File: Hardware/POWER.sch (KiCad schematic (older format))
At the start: 27 parts, among them J1 ATX24, J2 ATX24, P1 RCA_STEREO_JACK, P3 3.5mm_Audio, P4 3.5mm_Audio, Q2 BSS138, SW1 PWR_BTN, U2 LP38692, U3 PLR135/T10, U4 POM-3535L-3-R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

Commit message: Fixing schematic issues
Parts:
- removed D3, D4: LED, symbol LED-RESCUE-museV2
- removed J1, J2: ATX24, symbol ATX24
- removed R6, R7: 470, symbol R-RESCUE-museV2
- added P2: +12V, symbol CONN_01X01
- added P43: +5V, symbol CONN_01X01
- added P44: +12V_AUX, symbol CONN_01X01
- added P45: +5V_AUX, symbol CONN_01X01
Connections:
- net labels added: EDISON_RST_OUT
- net labels removed: +3.3V, ATX_PS_1_OK, ATX_PS_2_OK, ATX_PS_ON, EDISON_RST_OUT(1.8)
- wire segments 134 -> 79
- no-connect marks 9 -> 0
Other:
- note added: "Power Connectors"
- note removed: "ATX Power Connectors"
- note removed: "ATX Power Indicators"

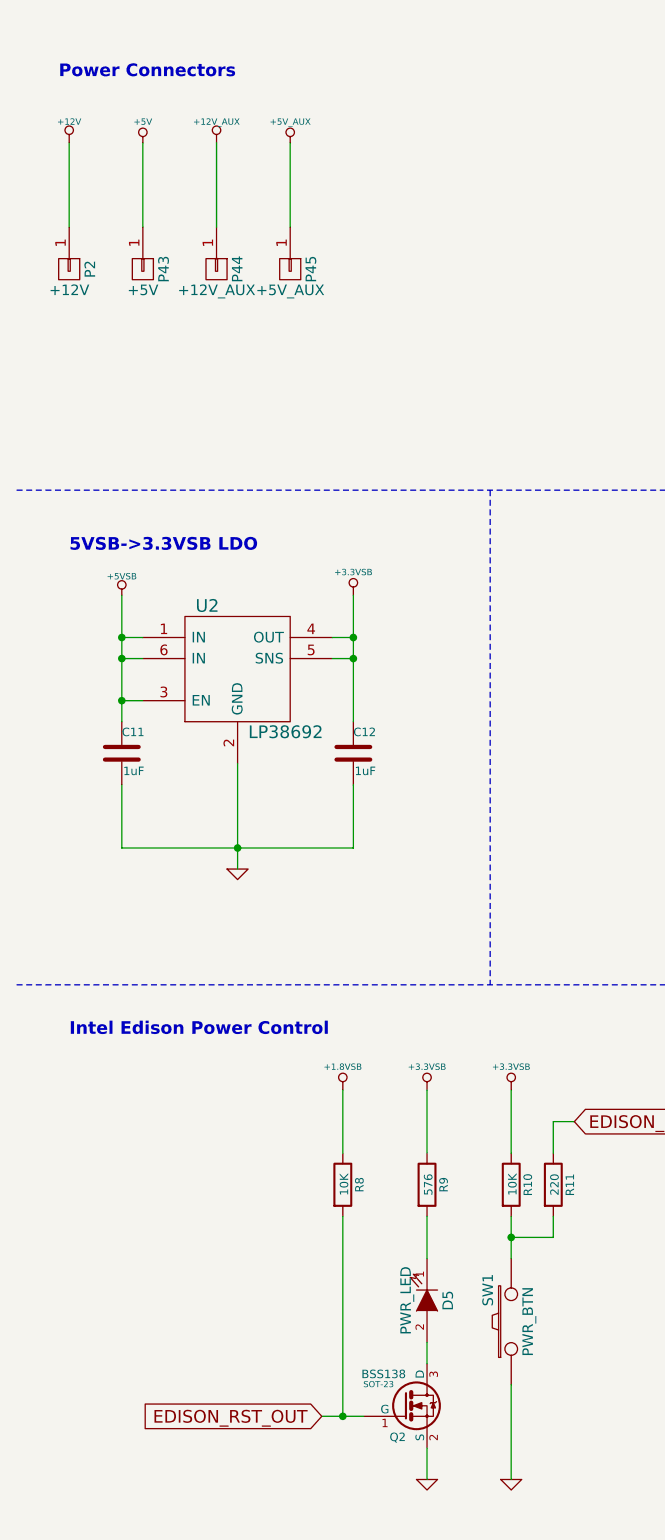
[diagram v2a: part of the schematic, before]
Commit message: Fixed schematic errors, added muse-v2-lib
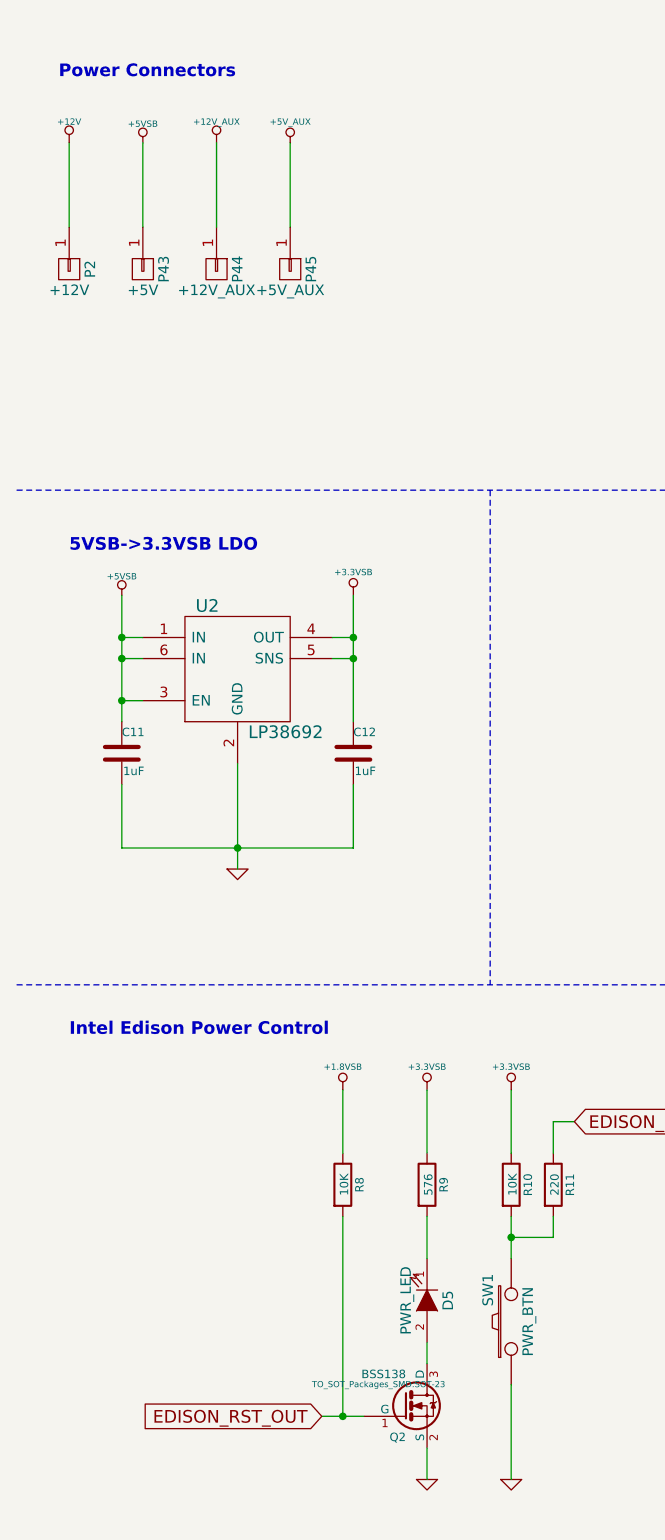
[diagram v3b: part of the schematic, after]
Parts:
- C11, C12, C13, C14: footprint (none) -> Capacitors_SMD:C_0402
- D5: footprint (none) -> LEDs:LED_0805
- P1: footprint (none) -> Choke_SMD:Choke_SMD_7.3x7.3_H3.5
- P43, P44, P45: footprint (none) -> Pin_Headers:Pin_Header_Straight_1x01
- Q2: footprint SOT-23 -> TO_SOT_Packages_SMD:SOT-23
- R10, R11, R8, R9: footprint (none) -> Resistors_SMD:R_0402
- SW1, U2, U3: footprint (none) -> MF_Switches:MF_Switches-TACT4.2MM
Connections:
- net +5V: no longer P43.1 (P1)
- net +5VSB: now also P43.1 (P1)

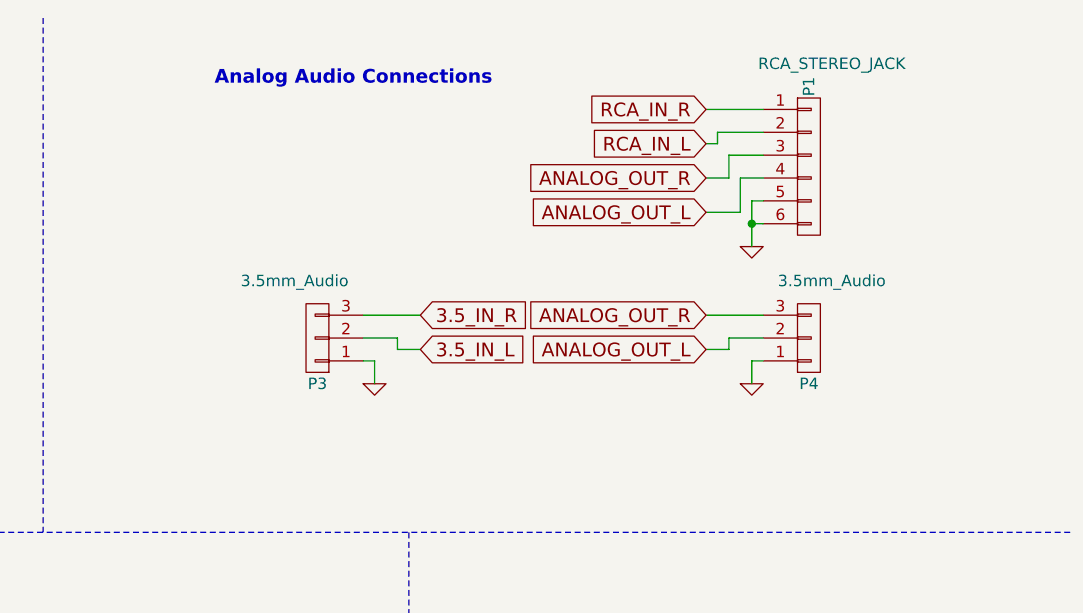
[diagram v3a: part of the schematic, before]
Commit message: Added proper audio connectors to schematic
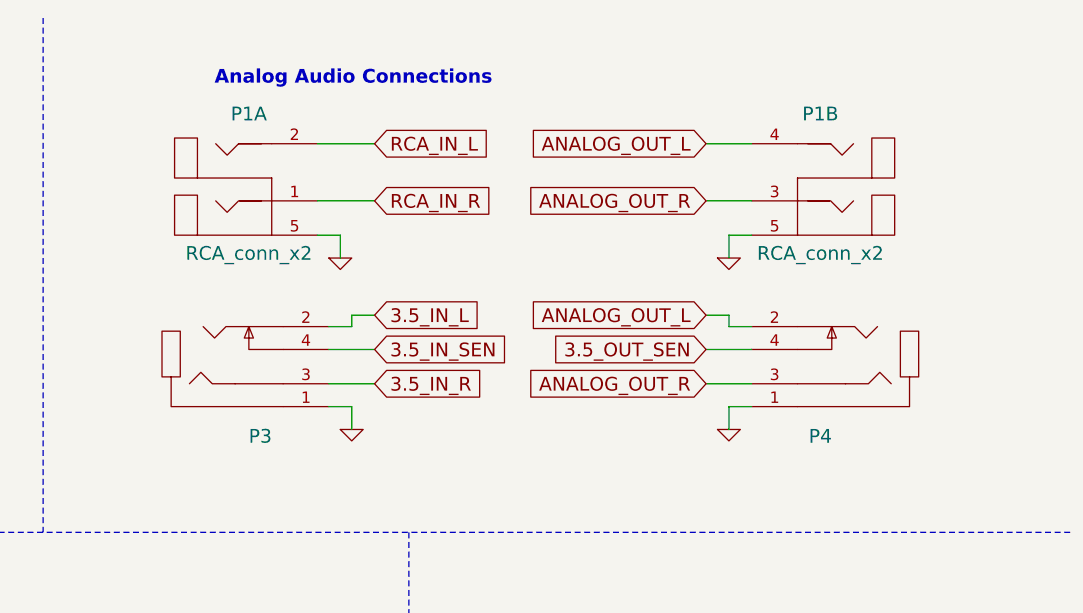
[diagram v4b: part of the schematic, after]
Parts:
- removed P1: RCA_STEREO_JACK, Choke_SMD:Choke_SMD_7.3x7.3_H3.5, symbol CONN_01X06
- removed P3, P4: 3.5mm_Audio, symbol CONN_01X03
- added P1: RCA_conn_x2, muse-v2-lib:PJRAS2X2S01X, symbol RCA_conn_x2
- added P3, P4: 3.5mm_conn_tip_switch, muse-v2-lib:3.5MM-AUDIO-SMD, symbol 3.5mm_conn_tip_switch
- P2: footprint (none) -> Pin_Headers:Pin_Header_Straight_1x01
- U2: footprint MF_Switches:MF_Switches-TACT4.2MM -> muse-v2-lib:WSON6
- U3: footprint MF_Switches:MF_Switches-TACT4.2MM -> muse-v2-lib:PLT133-T10W
- U4, U5, U7, U8: footprint (none) -> muse-v2-lib:POM-3535L-3-R
- U6: footprint (none) -> muse-v2-lib:PLT133-T10W
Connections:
- net 3.5_IN_L: now also P3.2
- net 3.5_IN_R: now also P3.3
- net ANALOG_OUT_L: now also P1.4, P4.2
- net ANALOG_OUT_R: now also P1.3, P4.3
- net GND: now also P1.5, P1.5, P3.1, P4.1
- net RCA_IN_L: now also P1.2
- net RCA_IN_R: now also P1.1
- new net 3.5_IN_SEN: P3.4
- new net 3.5_OUT_SEN: P4.4

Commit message: PCB Layout progress - placing PCM9211 components
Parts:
- U4, U5, U7, U8: footprint muse-v2-lib:POM-3535L-3-R -> muse-v2-lib:Pin_Header_Straight_1x02_MIC
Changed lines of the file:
@@
 F 0 "U4" H 9750 4100 60  0000 C CNN
 F 1 "POM-3535L-3-R" H 9900 3600 60  0000 C CNN
-F 2 "muse-v2-lib:POM-3535L-3-R" H 9900 3850 60  0001 C CNN
+F 2 "muse-v2-lib:Pin_Header_Straight_1x02_MIC" H 9900 3850 60  0001 C CNN
 F 3 "" H 9900 3850 60  0000 C CNN
 	1    9900 3850
@@
 F 0 "U5" H 9750 4700 60  0000 C CNN
 F 1 "POM-3535L-3-R" H 9900 4200 60  0000 C CNN
-F 2 "muse-v2-lib:POM-3535L-3-R" H 9900 4450 60  0001 C CNN
+F 2 "muse-v2-lib:Pin_Header_Straight_1x02_MIC" H 9900 4450 60  0001 C CNN
 F 3 "" H 9900 4450 60  0000 C CNN
 	1    9900 4450
@@
 F 0 "U7" H 9750 5300 60  0000 C CNN
 F 1 "POM-3535L-3-R" H 9900 4800 60  0000 C CNN
-F 2 "muse-v2-lib:POM-3535L-3-R" H 9900 5050 60  0001 C CNN
+F 2 "muse-v2-lib:Pin_Header_Straight_1x02_MIC" H 9900 5050 60  0001 C CNN
 F 3 "" H 9900 5050 60  0000 C CNN
 	1    9900 5050
@@
 F 0 "U8" H 9750 5900 60  0000 C CNN
 F 1 "POM-3535L-3-R" H 9900 5400 60  0000 C CNN
-F 2 "muse-v2-lib:POM-3535L-3-R" H 9900 5650 60  0001 C CNN
+F 2 "muse-v2-lib:Pin_Header_Straight_1x02_MIC" H 9900 5650 60  0001 C CNN
 F 3 "" H 9900 5650 60  0000 C CNN
 	1    9900 5650

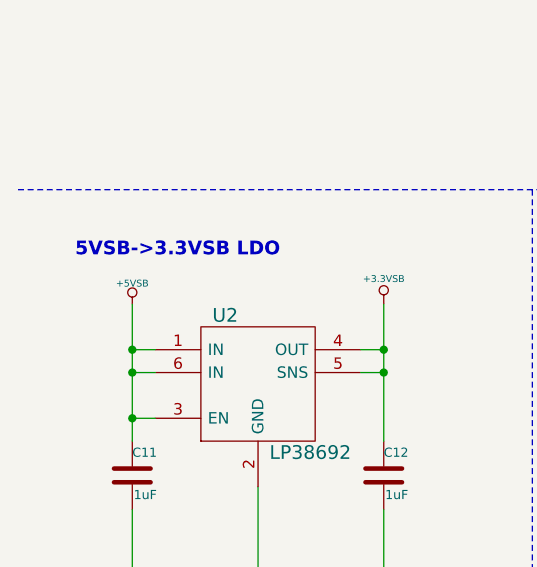
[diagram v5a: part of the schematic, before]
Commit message: Completed placement of level shifters
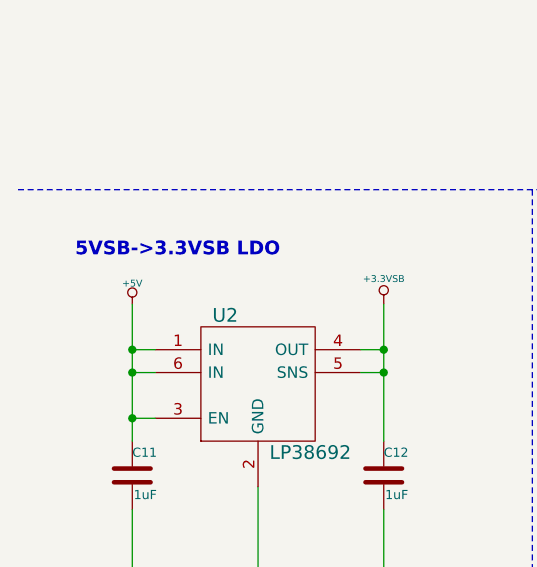
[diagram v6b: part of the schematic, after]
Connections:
- net +5V: now also C11.1, U2.1 (IN), U2.3 (EN), U2.6 (IN)
- net +5VSB: no longer C11.1, U2.1 (IN), U2.3 (EN), U2.6 (IN)
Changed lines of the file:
@@
 $EndComp
 $Comp
-L +5VSB #PWR020
-U 1 1 57EB078C
-P 1000 3250
-F 0 "#PWR020" H 1000 3340 20  0001 C CNN
-F 1 "+5VSB" H 1000 3340 30  0000 C CNN
-F 2 "" H 1000 3250 60  0000 C CNN
-F 3 "" H 1000 3250 60  0000 C CNN
-	1    1000 3250
-	1    0    0    -1
-$EndComp
-$Comp
-L GND-RESCUE-museV2-RESCUE-museV2 #PWR021
+L GND-RESCUE-museV2-RESCUE-museV2 #PWR020
 U 1 1 57EB079A
 P 1550 4550
-F 0 "#PWR021" H 1550 4550 30  0001 C CNN
+F 0 "#PWR020" H 1550 4550 30  0001 C CNN
 F 1 "GND" H 1550 4480 30  0001 C CNN
 F 2 "" H 1550 4550 60  0000 C CNN
@@
 Connection ~ 2100 3450
 $Comp
-L +12V #PWR022
+L +12V #PWR021
 U 1 1 57EB439D
 P 750 1100
-F 0 "#PWR022" H 750 1050 20  0001 C CNN
+F 0 "#PWR021" H 750 1050 20  0001 C CNN
 F 1 "+12V" H 750 1200 30  0000 C CNN
 F 2 "" H 750 1100 60  0000 C CNN
@@
 Power Connectors
 $Comp
-L +12V_AUX #PWR023
+L +12V_AUX #PWR022
 U 1 1 57EB43C6
 P 1450 1100
-F 0 "#PWR023" H 1450 1050 20  0001 C CNN
+F 0 "#PWR022" H 1450 1050 20  0001 C CNN
 F 1 "+12V_AUX" H 1450 1200 30  0000 C CNN
 F 2 "" H 1450 1100 60  0000 C CNN
@@
 $EndComp
 $Comp
-L +5V_AUX #PWR024
+L +5V_AUX #PWR023
 U 1 1 57EB43D0
 P 1800 1100
-F 0 "#PWR024" H 1800 1190 20  0001 C CNN
+F 0 "#PWR023" H 1800 1190 20  0001 C CNN
 F 1 "+5V_AUX" H 1800 1200 30  0000 C CNN
 F 2 "" H 1800 1100 60  0000 C CNN
@@
 Optical In
 $Comp
-L +3.3VSB #PWR025
+L +3.3VSB #PWR024
 U 1 1 57F7D788
 P 7800 4950
-F 0 "#PWR025" H 7800 4910 30  0001 C CNN
+F 0 "#PWR024" H 7800 4910 30  0001 C CNN
 F 1 "+3.3VSB" H 7800 5060 30  0000 C CNN
 F 2 "" H 7800 4950 60  0000 C CNN
@@
 $EndComp
 $Comp
-L GND-RESCUE-museV2-RESCUE-museV2 #PWR026
+L GND-RESCUE-museV2-RESCUE-museV2 #PWR025
 U 1 1 57F7D78E
 P 7800 5500
-F 0 "#PWR026" H 7800 5500 30  0001 C CNN
+F 0 "#PWR025" H 7800 5500 30  0001 C CNN
 F 1 "GND" H 7800 5430 30  0001 C CNN
 F 2 "" H 7800 5500 60  0000 C CNN
@@
 $EndComp
 $Comp
-L GND-RESCUE-museV2-RESCUE-museV2 #PWR027
+L GND-RESCUE-museV2-RESCUE-museV2 #PWR026
 U 1 1 57F7D796
 P 6150 4300
-F 0 "#PWR027" H 6150 4300 30  0001 C CNN
+F 0 "#PWR026" H 6150 4300 30  0001 C CNN
 F 1 "GND" H 6150 4230 30  0001 C CNN
 F 2 "" H 6150 4300 60  0000 C CNN
@@
 $EndComp
 $Comp
-L +3.3VSB #PWR028
+L +3.3VSB #PWR027
 U 1 1 57F7D79C
 P 6150 3750
-F 0 "#PWR028" H 6150 3710 30  0001 C CNN
+F 0 "#PWR027" H 6150 3710 30  0001 C CNN
 F 1 "+3.3VSB" H 6150 3860 30  0000 C CNN
 F 2 "" H 6150 3750 60  0000 C CNN
@@
 Analog Audio Connections
 $Comp
-L GND-RESCUE-museV2-RESCUE-museV2 #PWR029
+L GND-RESCUE-museV2-RESCUE-museV2 #PWR028
 U 1 1 57F7D7C3
 P 8050 2300
-F 0 "#PWR029" H 8050 2300 30  0001 C CNN
+F 0 "#PWR028" H 8050 2300 30  0001 C CNN
 F 1 "GND" H 8050 2230 30  0001 C CNN
 F 2 "" H 8050 2300 60  0000 C CNN
@@
 $EndComp
 $Comp
-L GND-RESCUE-museV2-RESCUE-museV2 #PWR030
+L GND-RESCUE-museV2-RESCUE-museV2 #PWR029
 U 1 1 57F7D7D4
 P 9700 2300
-F 0 "#PWR030" H 9700 2300 30  0001 C CNN
+F 0 "#PWR029" H 9700 2300 30  0001 C CNN
 F 1 "GND" H 9700 2230 30  0001 C CNN
 F 2 "" H 9700 2300 60  0000 C CNN
@@
 $EndComp
 $Comp
-L GND-RESCUE-museV2-RESCUE-museV2 #PWR031
+L GND-RESCUE-museV2-RESCUE-museV2 #PWR030
 U 1 1 57F7D80B
 P 10500 5850
-F 0 "#PWR031" H 10500 5850 30  0001 C CNN
+F 0 "#PWR030" H 10500 5850 30  0001 C CNN
 F 1 "GND" H 10500 5780 30  0001 C CNN
 F 2 "" H 10500 5850 60  0000 C CNN
@@
 MIC_4
 $Comp
-L GND-RESCUE-museV2-RESCUE-museV2 #PWR032
+L GND-RESCUE-museV2-RESCUE-museV2 #PWR031
 U 1 1 57FA222D
 P 6450 7350
-F 0 "#PWR032" H 6450 7350 30  0001 C CNN
+F 0 "#PWR031" H 6450 7350 30  0001 C CNN
 F 1 "GND" H 6450 7280 30  0001 C CNN
 F 2 "" H 6450 7350 60  0000 C CNN
@@
 $EndComp
 $Comp
-L +3.3VSB #PWR033
+L +3.3VSB #PWR032
 U 1 1 57FA223A
 P 6450 6250
-F 0 "#PWR033" H 6450 6210 30  0001 C CNN
+F 0 "#PWR032" H 6450 6210 30  0001 C CNN
 F 1 "+3.3VSB" H 6450 6360 30  0000 C CNN
 F 2 "" H 6450 6250 60  0000 C CNN
@@
 $EndComp
 $Comp
-L GND-RESCUE-museV2-RESCUE-museV2 #PWR034
+L GND-RESCUE-museV2-RESCUE-museV2 #PWR033
 U 1 1 57FA2240
 P 6150 7350
-F 0 "#PWR034" H 6150 7350 30  0001 C CNN
+F 0 "#PWR033" H 6150 7350 30  0001 C CNN
 F 1 "GND" H 6150 7280 30  0001 C CNN
 F 2 "" H 6150 7350 60  0000 C CNN
@@
 $EndComp
 $Comp
-L +3.3VSB #PWR035
+L +3.3VSB #PWR034
 U 1 1 57FA224D
 P 6150 6250
-F 0 "#PWR035" H 6150 6210 30  0001 C CNN
+F 0 "#PWR034" H 6150 6210 30  0001 C CNN
 F 1 "+3.3VSB" H 6150 6360 30  0000 C CNN
 F 2 "" H 6150 6250 60  0000 C CNN
@@
 	1800 1100 1800 1500
 $Comp
-L +5VSB #PWR036
+L +5VSB #PWR035
 U 1 1 5859E2FF
 P 1100 1100
-F 0 "#PWR036" H 1100 1190 20  0001 C CNN
+F 0 "#PWR035" H 1100 1190 20  0001 C CNN
 F 1 "+5VSB" H 1100 1190 30  0000 C CNN
 F 2 "" H 1100 1100 60  0000 C CNN
@@
 	9600 1300 9800 1300
 $Comp
-L GND-RESCUE-museV2-RESCUE-museV2 #PWR037
+L GND-RESCUE-museV2-RESCUE-museV2 #PWR036
 U 1 1 585AD273
 P 9700 1550
-F 0 "#PWR037" H 9700 1550 30  0001 C CNN
+F 0 "#PWR036" H 9700 1550 30  0001 C CNN
 F 1 "GND" H 9700 1480 30  0001 C CNN
 F 2 "" H 9700 1550 60  0000 C CNN
@@
 	9700 1550 9700 1450
 $Comp
-L GND-RESCUE-museV2-RESCUE-museV2 #PWR038
+L GND-RESCUE-museV2-RESCUE-museV2 #PWR037
 U 1 1 585AD9C8
 P 8000 1550
-F 0 "#PWR038" H 8000 1550 30  0001 C CNN
+F 0 "#PWR037" H 8000 1550 30  0001 C CNN
 F 1 "GND" H 8000 1480 30  0001 C CNN
 F 2 "" H 8000 1550 60  0000 C CNN
@@
 Wire Wire Line
 	8000 1450 7900 1450
+$Comp
+L +5V #PWR038
+U 1 1 58627E51
+P 1000 3250
+F 0 "#PWR038" H 1000 3340 20  0001 C CNN
+F 1 "+5V" H 1000 3340 30  0000 C CNN
+F 2 "" H 1000 3250 60  0000 C CNN
+F 3 "" H 1000 3250 60  0000 C CNN
+	1    1000 3250
+	1    0    0    -1
+$EndComp
 $EndSCHEMATC
